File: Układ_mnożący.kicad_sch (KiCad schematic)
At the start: 48 parts, among them IC1 LMC7660IM_NOPB, J1 Conn_01x02_Male, J2 Conn_01x01_Male, J3 Conn_01x01_Male, J4 Conn_01x01_Male, J5 Conn_01x01_Male, J6 Conn_01x01_Male, J7 Conn_01x01_Male, Q1 DMG1012UW, U1 TLC2272ACD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

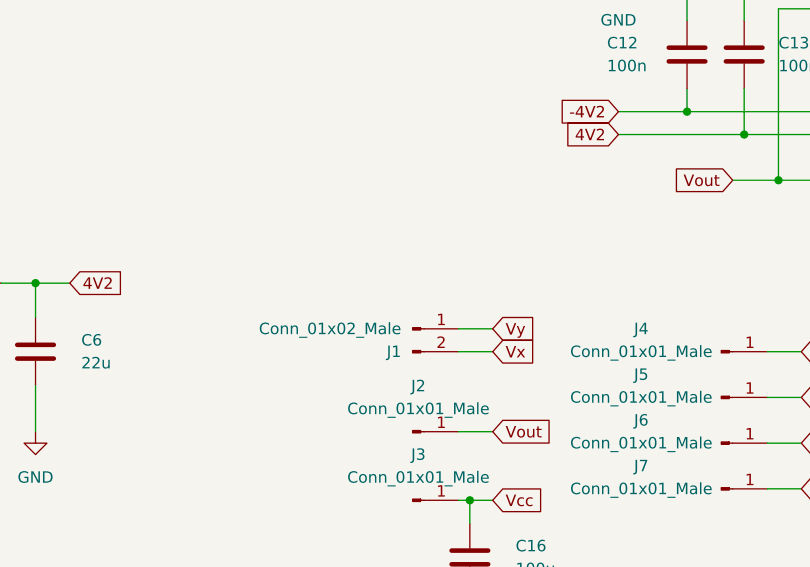
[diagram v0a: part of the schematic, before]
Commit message: Final Electrical Schematic v2
Added pinout to Vref
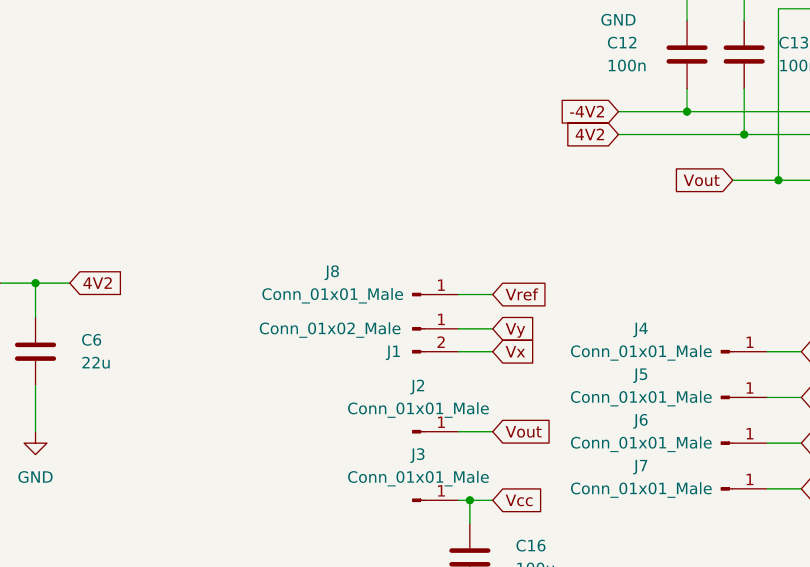
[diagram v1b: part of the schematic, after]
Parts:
- added J8: Conn_01x01_Male, Connector_PinHeader_2.54mm:PinHeader_1x01_P2.54mm_Vertical, symbol Connector:Conn_01x01_Male
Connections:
- net Vref: now also J8.1 (Pin_1)
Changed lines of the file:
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@@
+    (stroke (width 0) (type default) (color 0 0 0 0))
+  )
+  (wire (pts (xy 163.83 127) (xy 167.64 127))
     (stroke (width 0) (type default) (color 0 0 0 0))
   )
@@
     (effects (font (size 1.27 1.27)) (justify left))
     (property "Intersheet References" "${INTERSHEET_REFS}" (id 0) (at 175.1331 44.3706 0)
+      (effects (font (size 1.27 1.27)) (justify left) hide)
+    )
+  )
+  (global_label "Vref" (shape input) (at 167.64 127 0) (fields_autoplaced)
+    (effects (font (size 1.27 1.27)) (justify left))
+    (property "Intersheet References" "${INTERSHEET_REFS}" (id 0) (at 173.7421 127.0794 0)
       (effects (font (size 1.27 1.27)) (justify left) hide)
     )
@@
     (pin "1")
   )
+  (symbol (lib_id "Connector:Conn_01x01_Male") (at 158.75 127 0) (unit 1)
+    (in_bom yes) (on_board yes)
+    (property "Reference" "J8" (id 0) (at 149.86 124.46 0))
+    (property "Value" "Conn_01x01_Male" (id 1) (at 149.86 127 0))
+    (property "Footprint" "Connector_PinHeader_2.54mm:PinHeader_1x01_P2.54mm_Vertical" (id 2) (at 158.75 127 0)
+      (effects (font (size 1.27 1.27)) hide)
+    )
+    (property "Datasheet" "~" (id 3) (at 158.75 127 0)
+      (effects (font (size 1.27 1.27)) hide)
+    )
+    (pin "1")
+  )
   (symbol (lib_id "Device:C_Polarized") (at 68.58 173.99 0) (unit 1)
     (in_bom yes) (on_board yes)
@@
       (reference "J7") (unit 1) (value "Conn_01x01_Male") (footprint "Connector_PinHeader_2.54mm:PinHeader_1x01_P2.54mm_Vertical")
     )
+    (path "/b37af4b8-0d40-424b-bdeb-d476fc2c11ba"
+      (reference "J8") (unit 1) (value "Conn_01x01_Male") (footprint "Connector_PinHeader_2.54mm:PinHeader_1x01_P2.54mm_Vertical")
+    )
     (path "/65ff5319-9666-45f2-9ac3-4f23b299cea2"

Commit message: Final PCB design
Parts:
- removed J1: Conn_01x02_Male, Connector_PinHeader_2.54mm:PinHeader_1x02_P2.54mm_Vertical, symbol Connector:Conn_01x02_Male
- removed J3: Conn_01x01_Male, Connector_PinHeader_2.54mm:PinHeader_1x01_P2.54mm_Vertical, symbol Connector:Conn_01x01_Male
- added J1: Conn_01x01_Male, Connector_PinHeader_2.54mm:PinHeader_1x01_P2.54mm_Vertical, symbol Connector:Conn_01x01_Male
- added J3: Conn_01x02_Male, Connector_PinHeader_2.54mm:PinHeader_1x02_P2.54mm_Vertical, symbol Connector:Conn_01x02_Male
- C3, C5: footprint Capacitor_THT:CP_Radial_D5.0mm_P2.50mm -> Capacitor_SMD:C_1206_3216Metric_Pad1.33x1.80mm_HandSolder
- C6: footprint Capacitor_SMD:C_1206_3216Metric_Pad1.33x1.80mm_HandSolder -> Capacitor_Tantalum_SMD:CP_EIA-3528-21_Kemet-B
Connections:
- net GND: now also J3.1 (Pin_1)
- net V1: no longer RV2.3
- net Vcc: now also J3.2 (Pin_2)
- net Vref: no longer J8.1 (Pin_1), RV1.3
- net Vx: now also J8.1 (Pin_1)
- net Vy: now also J1.1 (Pin_1)
- net at R8.2, RV3.2: no longer RV3.1
- net at R10.1, RV4.2: no longer RV4.3
- no-connect marks 5 -> 9
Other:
- moved on the sheet: J7

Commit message: Final PCB design v2
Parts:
- added J9: Conn_01x01_Male, Connector_PinHeader_2.54mm:PinHeader_1x01_P2.54mm_Vertical, symbol Connector:Conn_01x01_Male
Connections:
- net -4V2: now also C13.2, U5.4 (VDD-/GND); no longer C12.2, U5.8 (VDD+)
- net 4V2: now also C12.2, U5.8 (VDD+); no longer C13.2, U5.4 (VDD-/GND)
- net Vref: now also J9.1 (Pin_1)
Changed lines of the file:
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@@
+    (stroke (width 0) (type default) (color 0 0 0 0))
+  )
+  (wire (pts (xy 200.66 153.67) (xy 201.93 153.67))
     (stroke (width 0) (type default) (color 0 0 0 0))
   )
@@
     )
   )
-  (global_label "4V2" (shape input) (at 181.61 109.22 180) (fields_autoplaced)
-    (effects (font (size 1.27 1.27)) (justify right))
-    (property "Intersheet References" "${INTERSHEET_REFS}" (id 0) (at 175.6893 109.2994 0)
-      (effects (font (size 1.27 1.27)) (justify right) hide)
-    )
-  )
   (global_label "-4V2" (shape input) (at 267.97 44.45 0) (fields_autoplaced)
     (effects (font (size 1.27 1.27)) (justify left))
@@
     )
   )
+  (global_label "-4V2" (shape input) (at 181.61 109.22 180) (fields_autoplaced)
+    (effects (font (size 1.27 1.27)) (justify right))
+    (property "Intersheet References" "${INTERSHEET_REFS}" (id 0) (at 174.1169 109.2994 0)
+      (effects (font (size 1.27 1.27)) (justify right) hide)
+    )
+  )
   (global_label "V4" (shape input) (at 255.27 114.3 0) (fields_autoplaced)
     (effects (font (size 1.27 1.27)) (justify left))
@@
     (effects (font (size 1.27 1.27)) (justify left))
     (property "Intersheet References" "${INTERSHEET_REFS}" (id 0) (at 175.1331 44.3706 0)
+      (effects (font (size 1.27 1.27)) (justify left) hide)
+    )
+  )
+  (global_label "Vref" (shape input) (at 201.93 153.67 0) (fields_autoplaced)
+    (effects (font (size 1.27 1.27)) (justify left))
+    (property "Intersheet References" "${INTERSHEET_REFS}" (id 0) (at 208.0321 153.7494 0)
       (effects (font (size 1.27 1.27)) (justify left) hide)
     )
@@
     )
   )
+  (global_label "4V2" (shape input) (at 181.61 106.68 180) (fields_autoplaced)
+    (effects (font (size 1.27 1.27)) (justify right))
+    (property "Intersheet References" "${INTERSHEET_REFS}" (id 0) (at 175.6893 106.7594 0)
+      (effects (font (size 1.27 1.27)) (justify right) hide)
+    )
+  )
   (global_label "Vout" (shape input) (at 167.64 142.24 0) (fields_autoplaced)
     (effects (font (size 1.27 1.27)) (justify left))
@@
     (property "Intersheet References" "${INTERSHEET_REFS}" (id 0) (at 36.7506 99.4893 90)
       (effects (font (size 1.27 1.27)) (justify left) hide)
-    )
-  )
-  (global_label "-4V2" (shape input) (at 181.61 106.68 180) (fields_autoplaced)
-    (effects (font (size 1.27 1.27)) (justify right))
-    (property "Intersheet References" "${INTERSHEET_REFS}" (id 0) (at 174.1169 106.7594 0)
-      (effects (font (size 1.27 1.27)) (justify right) hide)
     )
   )
@@
     (pin "1")
   )
+  (symbol (lib_id "Connector:Conn_01x01_Male") (at 195.58 153.67 0) (unit 1)
+    (in_bom yes) (on_board yes)
+    (property "Reference" "J9" (id 0) (at 186.69 151.13 0))
+    (property "Value" "Conn_01x01_Male" (id 1) (at 186.69 153.67 0))
+    (property "Footprint" "Connector_PinHeader_2.54mm:PinHeader_1x01_P2.54mm_Vertical" (id 2) (at 195.58 153.67 0)
+      (effects (font (size 1.27 1.27)) hide)
+    )
+    (property "Datasheet" "~" (id 3) (at 195.58 153.67 0)
+      (effects (font (size 1.27 1.27)) hide)
+    )
+    (pin "1")
+  )
   (symbol (lib_id "Device:R") (at 163.83 52.07 90) (unit 1)
     (in_bom yes) (on_board yes) (fields_autoplaced)
@@
       (reference "J8") (unit 1) (value "Conn_01x01_Male") (footprint "Connector_PinHeader_2.54mm:PinHeader_1x01_P2.54mm_Vertical")
     )
+    (path "/c9076186-9f2f-4344-a9b3-d8cd5c037540"
+      (reference "J9") (unit 1) (value "Conn_01x01_Male") (footprint "Connector_PinHeader_2.54mm:PinHeader_1x01_P2.54mm_Vertical")
+    )
     (path "/65ff5319-9666-45f2-9ac3-4f23b299cea2"
